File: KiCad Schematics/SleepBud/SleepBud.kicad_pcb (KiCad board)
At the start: 2 copper layers, 155 x 55 mm, 84 parts, among them J1 12V Barrel Jack, J2 USB_B_Micro, J3 1984798, J4 1984772, J5 1984772, Q1 FQP27P06, Q2 AO3400A, SW1 EN Button, SW2 Reset Button, U1 AMS1117-3.3, U2 AMS1117-5.0, U3 ESP32-S3-WROOM-1, U4 DS3231SN_, U5 TXS0108EPW

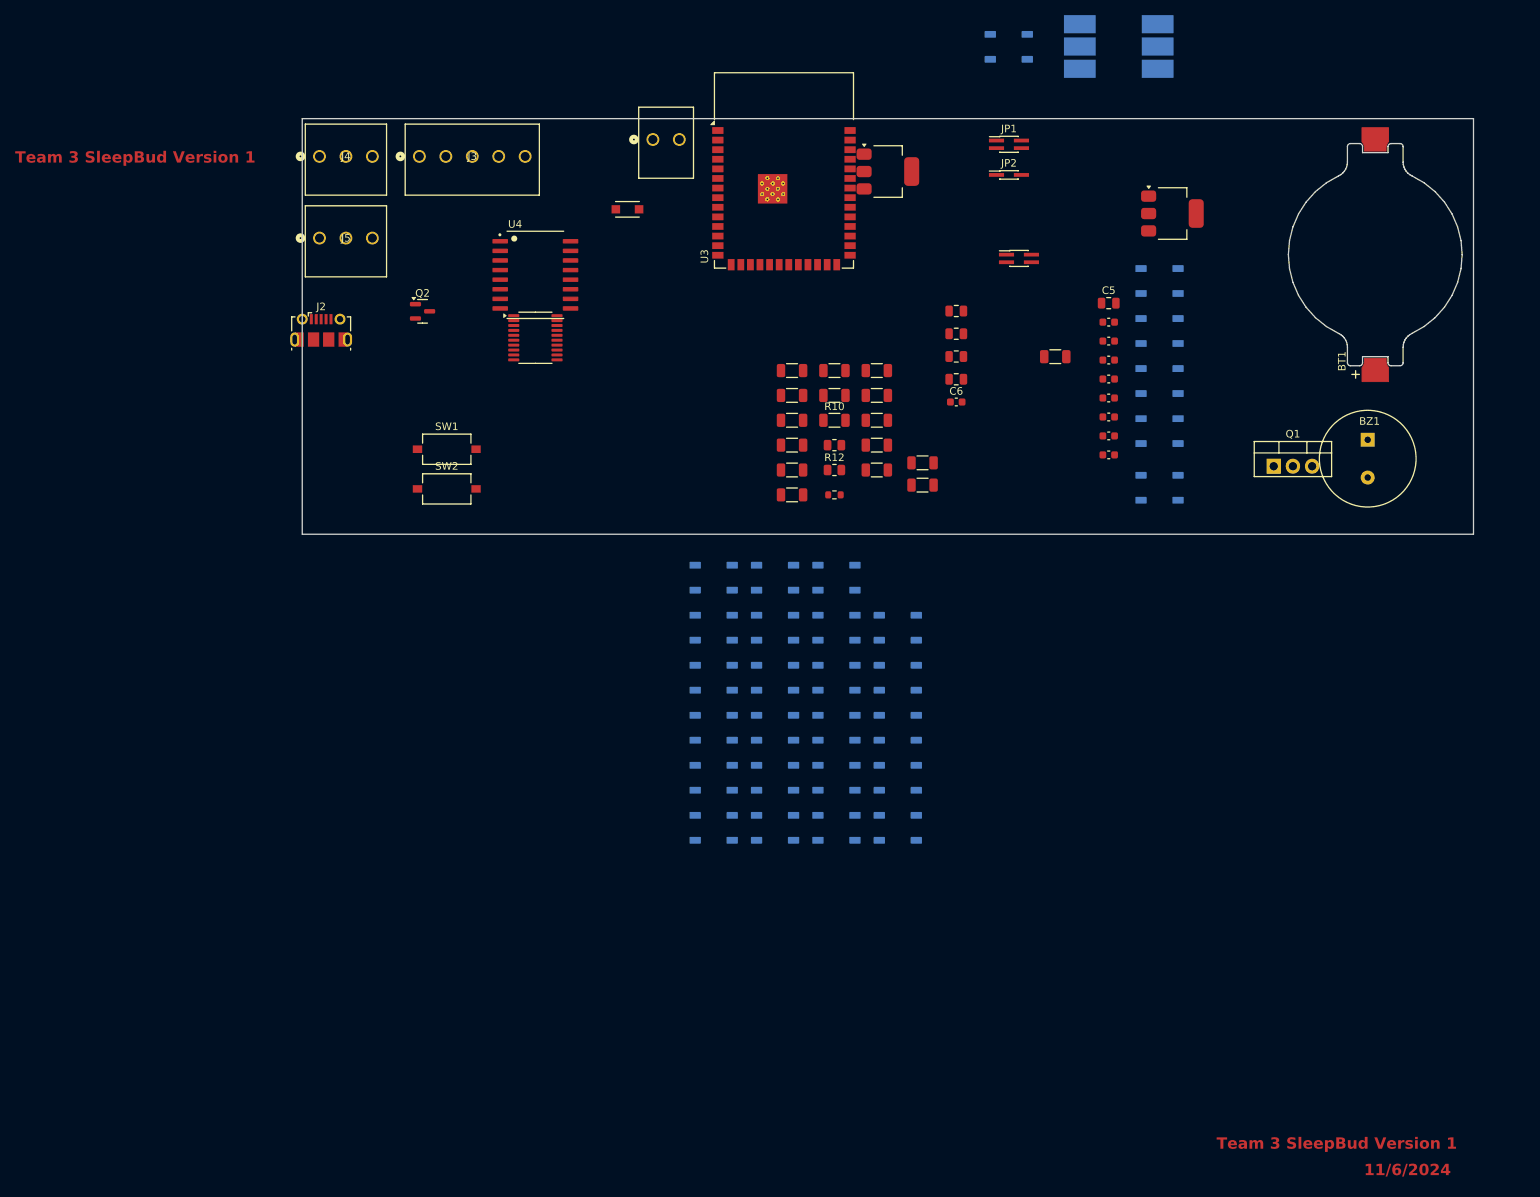
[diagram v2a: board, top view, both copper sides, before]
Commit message: Placed Parts to Potential area on Layout
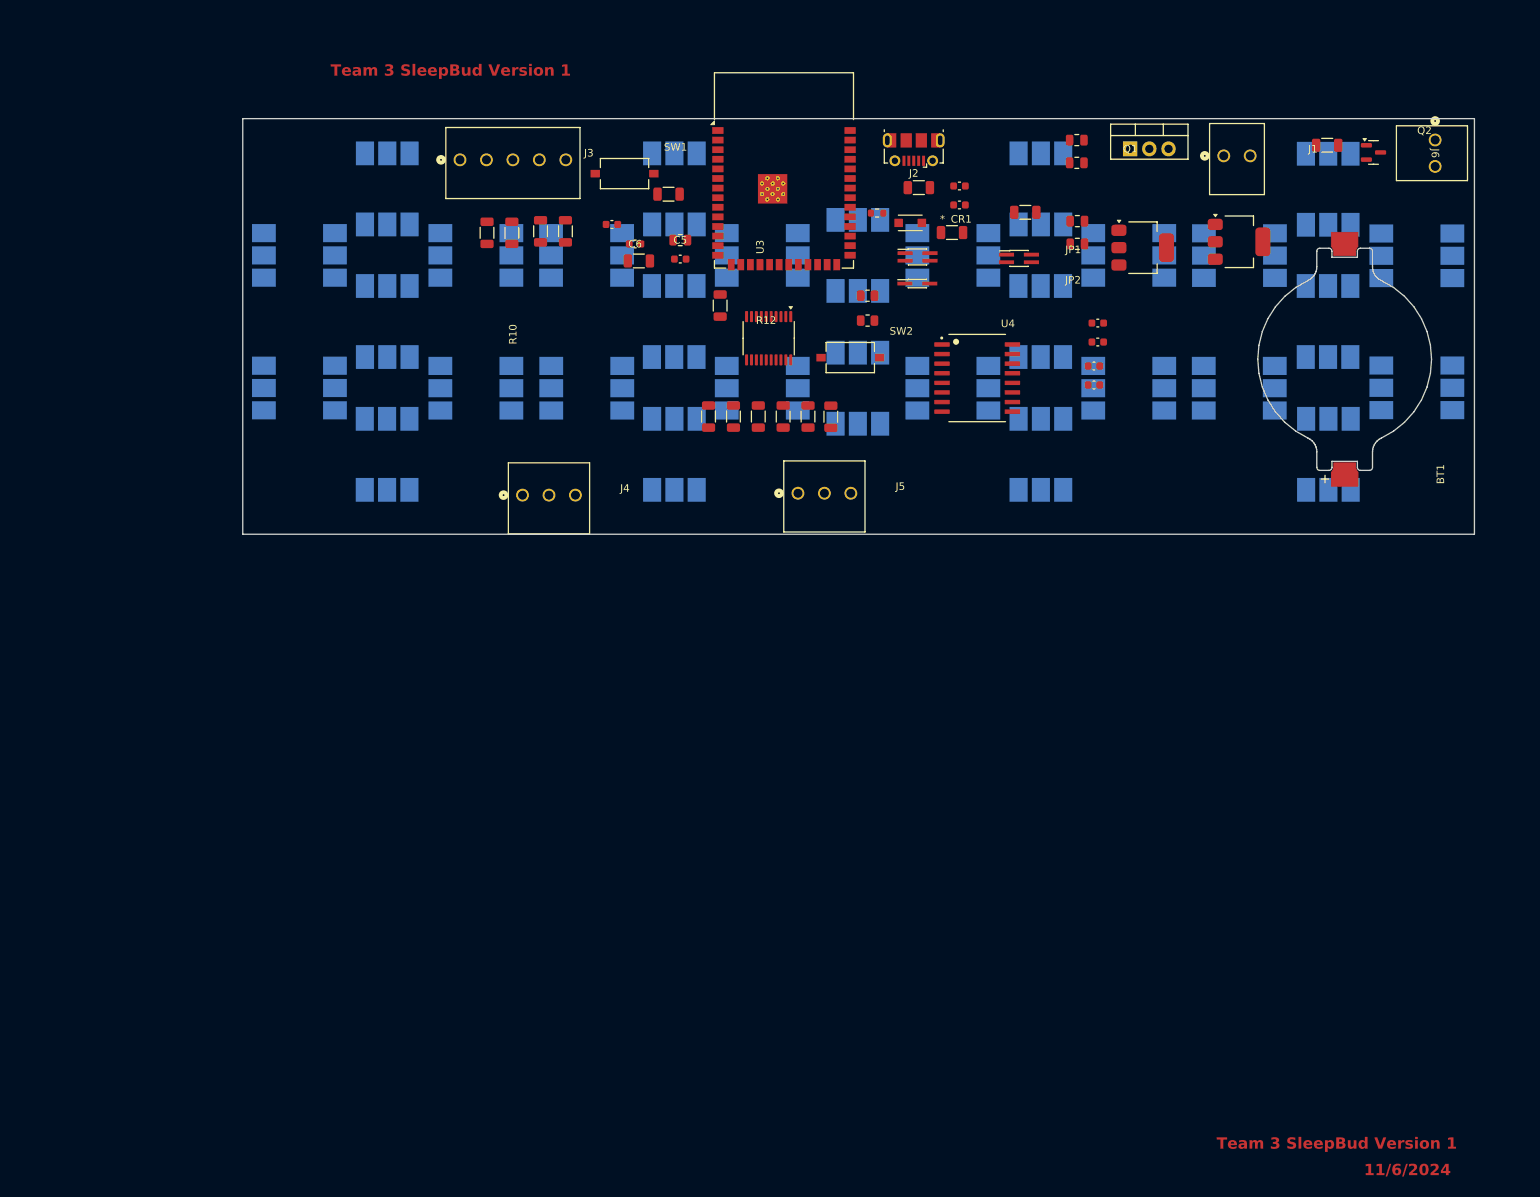
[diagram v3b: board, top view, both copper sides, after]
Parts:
- removed BZ1: PS1240P02BT, digikey-footprints:Piezo_Transducer_THT_PS1240P02BT
- added J6: Connector to Buzzer, 1984769:CONN_1984769_PXC, F.Cu at (215.9, 56.8)
- D1: footprint Custom:WB2812B -> Custom Pads:WB2812B
- D10, D11, D12, D13, D14, D15, D16, D17, D18, D19, D2, D20, D21, D22, D23, D24, D25, D26, D27, D28, D29, D3, D30, D4, D5, D6, D7, D8, D9: footprint LED_SMD:LED_WS2812B_PLCC4_5.0x5.0mm_P3.2mm -> Custom Pads:WB2812B
- J3: value 1984798 -> Button Connector
- J4: value 1984772 -> AM312 Connector
- J5: value 1984772 -> LED Lamp Connector
- moved Q2 127.6 mm to (207.8, 58.5)
- moved D24 98.9 mm to (77.2, 63.3), turned to -90 degrees
- moved D29 88.2 mm to (65.6, 72.1), turned to 0 degrees
- moved J2 82.0 mm to (146.9, 58.1), turned to 180 degrees
- moved D17 80.8 mm to (115.2, 63.3), turned to -90 degrees
- moved D30 79.7 mm to (77.2, 80.8), turned to -90 degrees
- moved D18 76.4 mm to (126.9, 72.1), turned to 0 degrees
- moved J1 75.6 mm to (187.9, 58.9)
- moved J5 71.8 mm to (131.6, 103.6)
- moved D28 70.9 mm to (65.6, 89.7)
- moved C8 67.5 mm to (107.0, 68.0)
- moved D22 67.3 mm to (103.6, 72.1), turned to 0 degrees
- moved D9 63.7 mm to (175.4, 72.1), turned to 0 degrees
- moved D23 61.8 mm to (115.2, 80.8), turned to -90 degrees
- moved D8 61.1 mm to (163.8, 63.3), turned to -90 degrees
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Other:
- board size 155 x 55 mm -> 163 x 55 mm

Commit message: Back of PCB Almost Done, Started on Front
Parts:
- BT1: footprint Battery:BatteryHolder_Keystone_1057_1x2032 -> BH74G5P:BH-74G-5-P_ADM
- moved C4 27.4 mm to (195.7, 63.3), turned to 180 degrees
- moved C3 26.4 mm to (192.7, 67.4), turned to -90 degrees
- moved BT1 21.0 mm to (188.8, 100.4), turned to 0 degrees
- moved CR1 11.2 mm to (155.9, 61.7)
- moved SW1 8.93 mm to (116.3, 56.6)
- moved U2 8.41 mm to (198.4, 70.0), turned to -90 degrees
- moved R13 7.16 mm to (149.2, 65.6)
- moved U3 6.44 mm to (136.2, 60.8)
- moved J3 5.88 mm to (92.7, 58.8)
- moved J2 5.30 mm to (152.2, 57.8)
- moved JP2 4.59 mm to (151.7, 77.5)
- moved U1 3.91 mm to (180.7, 69.3)
- moved JP1 3.85 mm to (151.3, 72.6)
- moved R8 0.96 mm to (148.6, 63.1)
- moved D12 0.54 mm to (151.6, 89.7)
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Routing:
- net +5V: track 0.00 -> 342.1 mm
- net +12V: track 0.00 -> 28.5 mm
- net Net-(D4-DOUT): track 0.00 -> 22.1 mm
- net Net-(D11-DOUT): track 0.00 -> 22.1 mm
- net Net-(D20-DOUT): track 0.00 -> 22.1 mm
- net Net-(D27-DOUT): track 0.00 -> 22.1 mm
- net Net-(D26-DOUT): track 0.00 -> 21.5 mm
- net Net-(D19-DOUT): track 0.00 -> 21.5 mm
- net Net-(D3-DOUT): track 0.00 -> 21.5 mm
- net Net-(D10-DOUT): track 0.00 -> 21.5 mm
- net Net-(D21-DOUT): track 0.00 -> 20.4 mm
- net Net-(D5-DOUT): track 0.00 -> 20.4 mm
- net Net-(D28-DOUT): track 0.00 -> 20.4 mm
- net Net-(D12-DOUT): track 0.00 -> 20.4 mm
- net Net-(D2-DOUT): track 0.00 -> 20.0 mm
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
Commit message: PCB Work on V1.1
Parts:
- moved Q1 58.3 mm to (141.0, 104.4)
- moved J1 57.3 mm to (152.1, 103.5)
- moved C4 51.5 mm to (163.7, 103.6), turned to -90 degrees
- moved J6 49.2 mm to (215.1, 106.5), turned to 90 degrees
- moved C3 45.7 mm to (167.7, 105.7), turned to 0 degrees
- moved R4 44.5 mm to (202.0, 102.0)
- moved Q2 44.3 mm to (207.8, 102.8)
- moved U2 41.7 mm to (170.4, 100.9), turned to 0 degrees
- moved BT1 39.0 mm to (204.4, 64.7)
- moved U1 36.4 mm to (151.4, 90.9)
- moved CR1 36.0 mm to (141.2, 94.6)
- moved R1 36.0 mm to (147.0, 99.3)
- moved U4 28.3 mm to (177.7, 71.0)
- moved C11 25.8 mm to (169.0, 55.4)
- moved C14 25.8 mm to (168.5, 63.5)
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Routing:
- net +5V: track 342.1 -> 509.3 mm, vias 0 -> 1
- net +12V: track 28.5 -> 81.8 mm
- net Net-(U3-IO7): track 0.00 -> 44.0 mm
- net Net-(U3-IO6): track 0.00 -> 38.1 mm
- net Net-(U3-IO5): track 0.00 -> 36.7 mm
- net Net-(U3-IO4): track 0.00 -> 31.6 mm
- net +3.3V: track 0.00 -> 23.0 mm
- net Net-(U3-EN): track 0.00 -> 14.3 mm
- net Net-(JP3-TDI): track 0.00 -> 7.85 mm, vias 0 -> 2
- net Net-(C8-Pad2): track 0.00 -> 7.74 mm
- net Net-(JP3-TCK): track 0.00 -> 7.41 mm
- net Net-(JP1-RXD0): track 0.00 -> 6.63 mm
- net Net-(Q2-D): track 0.00 -> 6.45 mm
- net Net-(JP1-TXD0): track 0.00 -> 4.88 mm
- net Net-(JP3-TMS): track 0.00 -> 4.01 mm
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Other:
- board text added: "Team 3 SleepBud Version 1.1"

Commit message: PCB Layout Routing Rough Draft Finished
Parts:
- U2: value AMS1117-5.0 -> AZ1084CD; footprint Package_TO_SOT_SMD:SOT-223-3_TabPin2 -> Custom Pads:AZ1084CD
- moved C10 92.6 mm to (65.0, 61.9), turned to 180 degrees
- moved R8 92.2 mm to (64.2, 64.1)
- moved C9 92.0 mm to (68.7, 61.9)
- moved J2 87.9 mm to (66.6, 57.9)
- moved R5 87.1 mm to (69.5, 64.0), turned to 180 degrees
- moved C1 37.1 mm to (147.9, 98.3), turned to -90 degrees
- moved C11 34.1 mm to (158.6, 87.9), turned to -90 degrees
- moved C14 33.1 mm to (140.4, 81.0)
- moved C13 32.7 mm to (140.5, 77.9)
- moved SW2 29.7 mm to (168.0, 89.0), turned to 180 degrees
- moved R13 22.4 mm to (161.4, 86.9), turned to 0 degrees
- moved C2 20.4 mm to (154.5, 85.3)
- moved C12 17.7 mm to (176.5, 73.9), turned to -90 degrees
- moved U4 16.6 mm to (163.9, 80.2), turned to 90 degrees
- moved R12 16.5 mm to (156.8, 73.4), turned to 90 degrees
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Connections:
- U4 pad 10: (no net) -> GND
- U4 pad 11: (no net) -> GND
- U4 pad 12: (no net) -> GND
- U4 pad 5: (no net) -> GND
- U4 pad 6: (no net) -> GND
- U4 pad 7: (no net) -> GND
- U4 pad 8: (no net) -> GND
- U4 pad 9: (no net) -> GND
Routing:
- net +3.3V: track 23.0 -> 218.5 mm, vias 0 -> 11
- net VBUS: track 0.00 -> 149.4 mm
- net Net-(D24-DIN): track 0.00 -> 93.7 mm, vias 0 -> 1
- net Net-(D1-DIN): track 0.00 -> 80.1 mm, vias 0 -> 3
- net Net-(D8-DIN): track 0.00 -> 73.7 mm, vias 0 -> 1
- net /Buzzer: track 0.00 -> 73.6 mm
- net Net-(U3-IO20): track 0.00 -> 73.3 mm, vias 0 -> 2
- net Net-(U3-IO19): track 0.00 -> 64.5 mm, vias 0 -> 2
- net Net-(U3-IO8): track 0.00 -> 56.2 mm
- net Net-(D17-DIN): track 0.00 -> 42.6 mm, vias 0 -> 1
- net Net-(U3-IO38): track 0.00 -> 37.2 mm, vias 0 -> 2
- net Net-(BT1-+): track 0.00 -> 32.9 mm
- net Net-(U3-IO37): track 0.00 -> 29.1 mm, vias 0 -> 2
- net Net-(D15-DIN): track 0.00 -> 26.9 mm, vias 0 -> 1
- net Net-(U3-IO36): track 0.00 -> 21.0 mm
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- added copper zone on B.Cu, net GND
- added copper zone on F.Cu, net GND
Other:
- board size 163 x 55 mm -> 165 x 55 mm
- board text added: "11/14/2024"
- board text removed: "11/6/2024"
- board text removed: "Team 3 SleepBud Version 1"

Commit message: change title for layput
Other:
- board text added: "Team 3 SleepBud Version 1.1 11/14/2024"
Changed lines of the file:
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@@
 		(tags "capacitor")
 		(property "Reference" "C9"
-			(at 0 -1.43 360)
+			(at 0 -1.43 0)
 			(layer "F.SilkS")
 			(hide yes)
@@
 		)
 		(property "Value" "22pF"
-			(at 0 1.43 360)
+			(at 0 1.43 0)
 			(layer "F.Fab")
 			(hide yes)
@@
 		)
 		(property "Footprint" "footprints:SDO_SOD-123FL498_OSI"
-			(at 0 0 360)
+			(at 0 0 0)
 			(layer "F.Fab")
 			(hide yes)
@@
 		)
 		(property "Datasheet" "MBR120LSFT3G"
-			(at 0 0 360)
+			(at 0 0 0)
 			(layer "F.Fab")
 			(hide yes)
@@
 		)
 		(property "Description" ""
-			(at 0 0 360)
+			(at 0 0 0)
 			(layer "F.Fab")
 			(hide yes)
@@
 		(tags "resistor")
 		(property "Reference" "R8"
-			(at 0 -1.82 360)
+			(at 0 -1.82 0)
 			(layer "F.SilkS")
 			(hide yes)
@@
 		)
 		(property "Value" "0"
-			(at 0 1.82 360)
+			(at 0 1.82 0)
 			(layer "F.Fab")
 			(hide yes)
@@
 		(tags "capacitor")
 		(property "Reference" "C13"
-			(at 0 -1.43 360)
+			(at 0 -1.43 0)
 			(layer "F.SilkS")
 			(hide yes)
@@
 		)
 		(property "Value" "0.1uF"
-			(at 0 1.43 360)
+			(at 0 1.43 0)
 			(layer "F.Fab")
 			(hide yes)
@@
 		(tags "resistor")
 		(property "Reference" "R14"
-			(at 0 -1.82 360)
+			(at 0 -1.82 0)
 			(layer "F.SilkS")
 			(hide yes)
@@
 		)
 		(property "Value" "10kOhm"
-			(at 0 1.82 360)
+			(at 0 1.82 0)
 			(layer "F.Fab")
 			(hide yes)
@@
 		(tags "capacitor")
 		(property "Reference" "C10"
-			(at 0 -1.43 360)
+			(at 0 -1.43 0)
 			(layer "F.SilkS")
 			(hide yes)
@@
 		)
 		(property "Value" "22pF"
-			(at 0 1.43 360)
+			(at 0 1.43 0)
 			(layer "F.Fab")
 			(hide yes)
@@
 		(tags "resistor")
 		(property "Reference" "R13"
-			(at 0 -1.43 360)
+			(at 0 -1.43 0)
 			(layer "F.SilkS")
 			(hide yes)
@@
 		)
 		(property "Value" "4.7k"
-			(at 0 1.43 360)
+			(at 0 1.43 0)
 			(layer "F.Fab")
 			(hide yes)
@@
 		(tags "resistor")
 		(property "Reference" "R5"
-			(at 0 -1.82 360)
+			(at 0 -1.82 0)
 			(layer "F.SilkS")
 			(hide yes)
@@
 		)
 		(property "Value" "0"
-			(at 0 1.82 360)
+			(at 0 1.82 0)
 			(layer "F.Fab")
 			(hide yes)
@@
 		)
 	)
-	(gr_text "Team 3 SleepBud Version 1.1\n"
-		(at 69.75 48.5 0)
+	(gr_text "11/14/2024"
+		(at 206.5 194 0)
 		(layer "F.Cu")
 		(effects
@@
 		)
 	)
-	(gr_text "11/14/2024"
-		(at 206.5 194 0)
-		(layer "F.Cu")
+	(gr_text "Team 3 SleepBud Version 1.1\n11/14/2024\n"
+		(at 58.48 104.1 0)
+		(layer "F.SilkS")
 		(effects
 			(font
